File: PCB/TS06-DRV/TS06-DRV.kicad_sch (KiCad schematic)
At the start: 0 parts

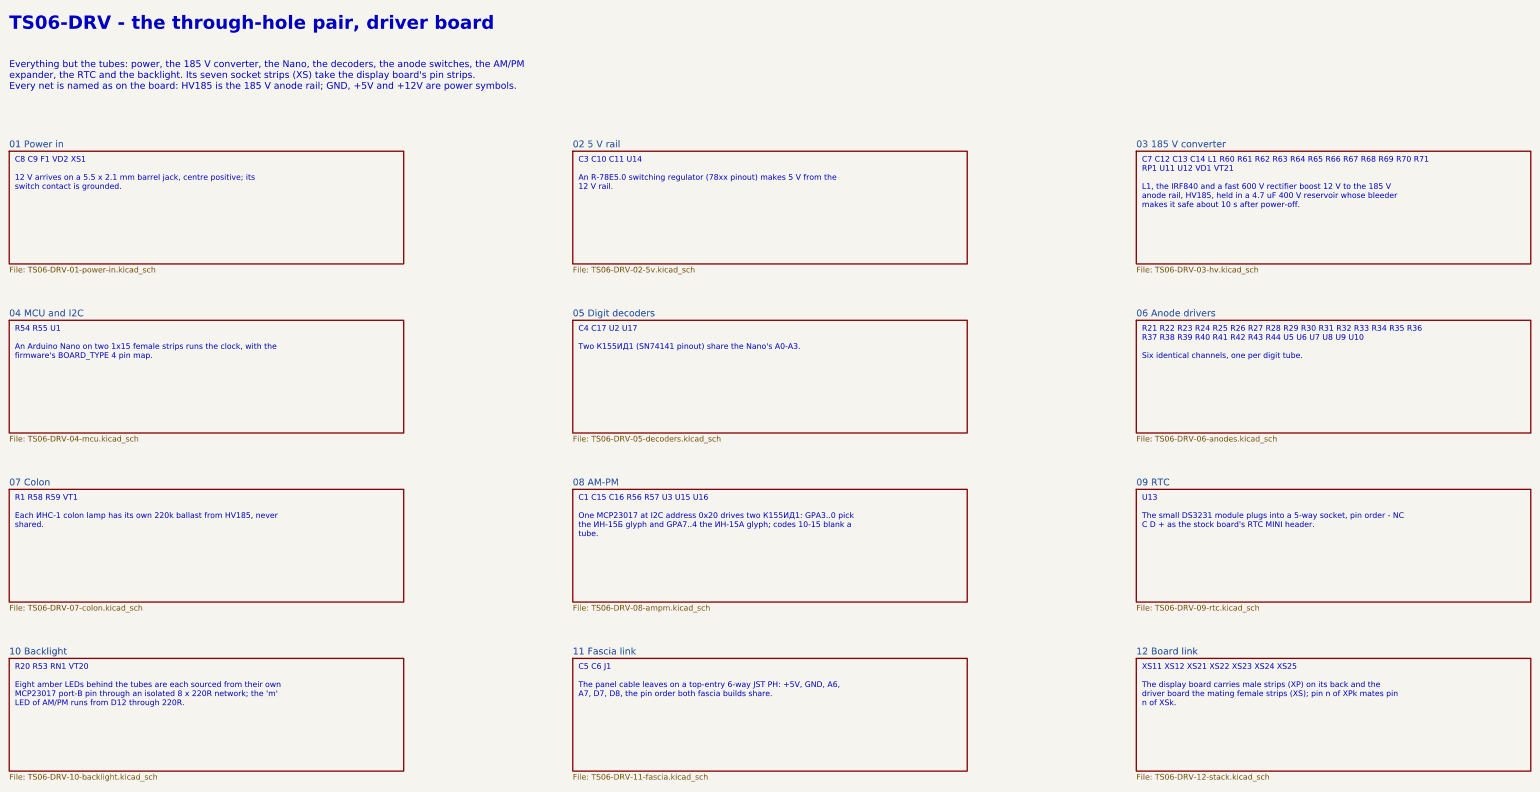
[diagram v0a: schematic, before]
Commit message: TS06-DRV rev B: routed - round 13, 0 nets sharing, 0 unrouted; board, rules and schematic written
The route of run r3 (PYTHONHASHSEED=0, the RC block of OPTIONS.md option 3),
polished (30 nets shorter), saved in tools/mkpcb_drv_routes.json, and the board
regenerated from it: check() 0 problems, 0 cathode pads under 0.5 mm, check_mate()
clean, 1164 segments, 0 vias. TS06-DRV.kicad_dru carries the 0.8 mm HV pad rule.
Schematic regenerated by tools/mksch_pair.py; BOMs unchanged by tools/bom_pair.py.

State: board written from a converged route; verify_pair not yet run.
Blocker: none.
Next: verify_pair.sh, scorecard, README row.

Co-Authored-By: Claude Opus 5.5 <noreply@anthropic.com>
Claude-Session: https://claude.ai/code/session_01WoV3gyAFgmtuk6W6Dr4bdA
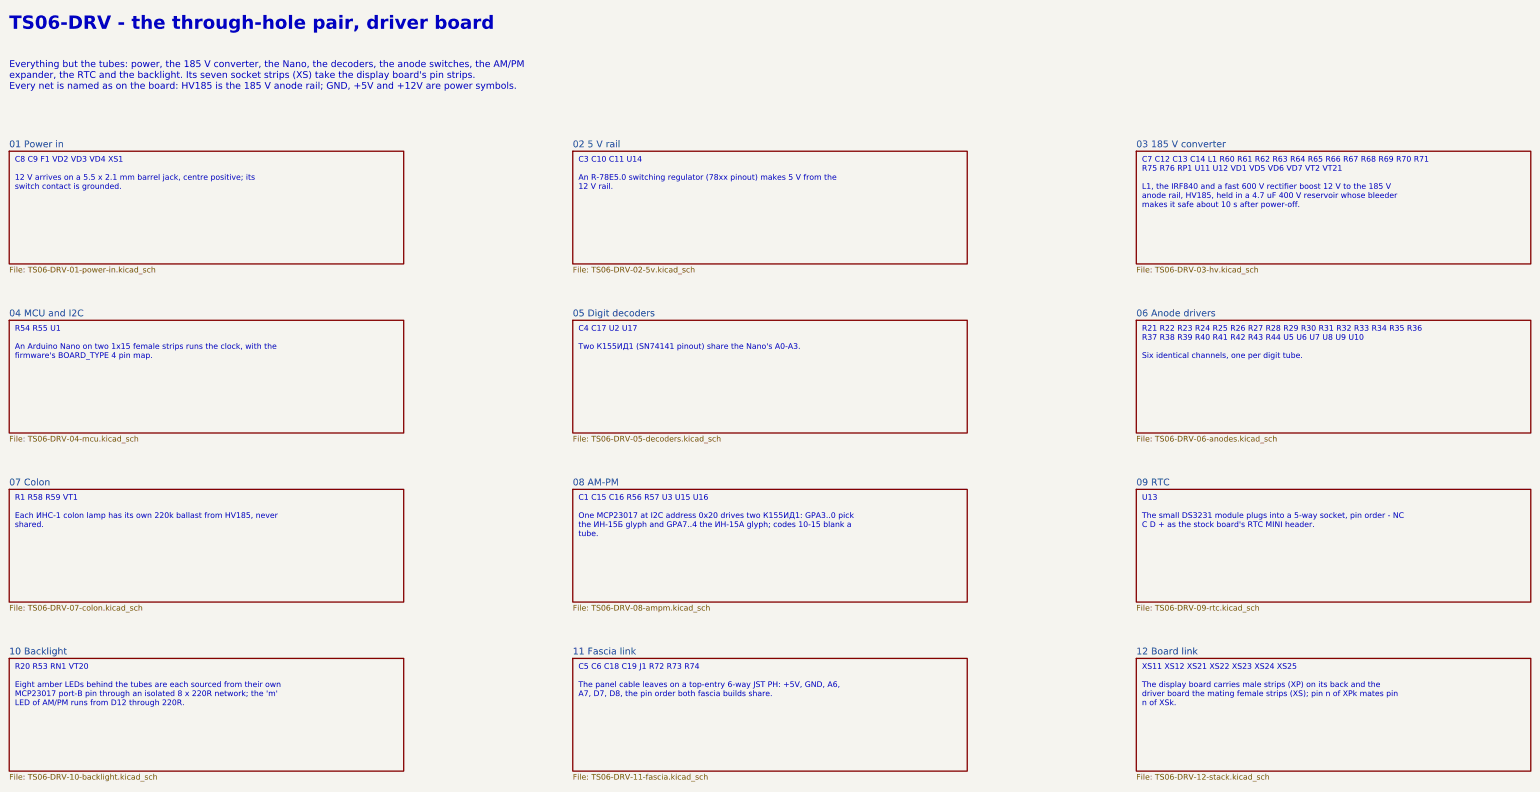
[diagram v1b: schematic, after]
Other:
- note added: "C5 C6 C18 C19 J1 R72 R73 R74 The panel cable leaves on a top-entry 6-way JST PH: +5V, GND, A6, A7, D7, D8, the pin order both fascia builds share."
- note added: "C7 C12 C13 C14 L1 R60 R61 R62 R63 R64 R65 R66 R67 R68 R69 R70 R71 R75 R76 RP1 U11 U12 VD1 VD5 VD6 VD7 VT2 VT21 L1, the IRF840 and a fast 600 V rectifier boost 12 V to the 185 V anode rail, HV185, held in a 4.7 uF 400 V reservoir whose bleeder makes it safe about 10 s after power-off."
- note added: "C8 C9 F1 VD2 VD3 VD4 XS1 12 V arrives on a 5.5 x 2.1 mm barrel jack, centre positive; its switch contact is grounded."
- note removed: "C5 C6 J1 The panel cable leaves on a top-entry 6-way JST PH: +5V, GND, A6, A7, D7, D8, the pin order both fascia builds share."
- note removed: "C7 C12 C13 C14 L1 R60 R61 R62 R63 R64 R65 R66 R67 R68 R69 R70 R71 RP1 U11 U12 VD1 VT21 L1, the IRF840 and a fast 600 V rectifier boost 12 V to the 185 V anode rail, HV185, held in a 4.7 uF 400 V reservoir whose bleeder makes it safe about 10 s after power-off."
- note removed: "C8 C9 F1 VD2 XS1 12 V arrives on a 5.5 x 2.1 mm barrel jack, centre positive; its switch contact is grounded."
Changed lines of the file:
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@@
 )
 )
-(text "C8 C9 F1 VD2 XS1\n\n12 V arrives on a 5.5 x 2.1 mm barrel jack, centre positive; its\nswitch contact is grounded."
+(text "C8 C9 F1 VD2 VD3 VD4 XS1\n\n12 V arrives on a 5.5 x 2.1 mm barrel jack, centre positive; its\nswitch contact is grounded."
 (exclude_from_sim no)
 (at 21.59 52.07 0)
@@
 )
 )
-(text "C7 C12 C13 C14 L1 R60 R61 R62 R63 R64 R65 R66 R67 R68 R69 R70 R71\nRP1 U11 U12 VD1 VT21\n\nL1, the IRF840 and a fast 600 V rectifier boost 12 V to the 185 V\nanode rail, HV185, held in a 4.7 uF 400 V reservoir whose bleeder\nmakes it safe about 10 s after power-off."
+(text "C7 C12 C13 C14 L1 R60 R61 R62 R63 R64 R65 R66 R67 R68 R69 R70 R71\nR75 R76 RP1 U11 U12 VD1 VD5 VD6 VD7 VT2 VT21\n\nL1, the IRF840 and a fast 600 V rectifier boost 12 V to the 185 V\nanode rail, HV185, held in a 4.7 uF 400 V reservoir whose bleeder\nmakes it safe about 10 s after power-off."
 (exclude_from_sim no)
 (at 275.59 52.07 0)
@@
 )
 )
-(text "C5 C6 J1\n\nThe panel cable leaves on a top-entry 6-way JST PH: +5V, GND, A6,\nA7, D7, D8, the pin order both fascia builds share."
+(text "C5 C6 C18 C19 J1 R72 R73 R74\n\nThe panel cable leaves on a top-entry 6-way JST PH: +5V, GND, A6,\nA7, D7, D8, the pin order both fascia builds share."
 (exclude_from_sim no)
 (at 148.59 166.37 0)
